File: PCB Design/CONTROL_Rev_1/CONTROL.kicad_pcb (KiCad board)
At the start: 2 copper layers, 40 x 80 mm, 42 parts, among them J1 Conn_01x24_Pin, J2 Conn_01x24_Pin, J3 Micro_SD_Card, P1 USB_C_Plug_USB2.0, SW1 SW_SPDT, U1 STM32F446RET6, Y1 16MHz, Y2 32.768KHz

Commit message: Completed Rev1 and Documentation
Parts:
- removed P1: USB_C_Plug_USB2.0, Connector_USB:USB_C_Receptacle_GCT_USB4085
- added D3: MINT, CONTROL:JB2835AWTWU57EA0000N0000001, F.Cu at (52.9, 157.6)
- added J4: USB_C_Receptacle_USB2.0_16P, Connector_USB:USB_C_Receptacle_GCT_USB4085, F.Cu at (75.6, 177.1)
- added R11: 5.1k, Resistor_SMD:R_0603_1608Metric, B.Cu at (73.9, 176.2)
- added R12: 5.1k, Resistor_SMD:R_0603_1608Metric, B.Cu at (78.4, 172.0)
- added R13: 1k, Resistor_SMD:R_0603_1608Metric, F.Cu at (52.8, 154.7)
- C1, C2, C3, C4, C5, C6, C7, C8, C9, R10, R2, R3, R4, R5, R6, R8, R9: moved to B.Cu
- C13, C14: footprint Capacitor_SMD:C_0603_1608Metric -> Capacitor_SMD:C_0402_1005Metric
- FB1: footprint Inductor_SMD:L_0201_0603Metric -> Inductor_SMD:L_0603_1608Metric; moved to B.Cu
- moved D1 22.5 mm to (62.1, 176.0), turned to -90 degrees
- moved R7 18.6 mm to (62.1, 173.0), turned to 180 degrees
- moved R5 13.2 mm to (51.5, 169.9), turned to 90 degrees
- moved R4 10.7 mm to (49.7, 171.7)
- moved R6 10.7 mm to (49.7, 168.5)
- moved R2 10.2 mm to (80.0, 148.4)
- moved C13 7.72 mm to (67.5, 145.0)
- moved C14 7.72 mm to (67.5, 143.3)
- moved C11 7.60 mm to (67.8, 140.3)
- moved C12 7.60 mm to (64.6, 140.3)
- moved Y1 7.60 mm to (65.3, 137.5)
- moved Y2 7.60 mm to (65.3, 144.2)
- moved R3 5.59 mm to (80.0, 152.6), turned to 90 degrees
- moved C1 4.09 mm to (70.3, 157.1), turned to -90 degrees
- moved C4 3.15 mm to (71.3, 166.1)
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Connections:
- net /LISTEN_EN renamed /PB5
- A1 pad 10: unconnected-(A1-GPIO7-Pad10) -> /GPIO_7
- A1 pad 11: unconnected-(A1-GPIO8-Pad11) -> /GPIO_8
- A1 pad 12: unconnected-(A1-GPIO9-Pad12) -> /GPIO_9
- A1 pad 14: unconnected-(A1-GPIO10-Pad14) -> /GPIO_10
- A1 pad 15: unconnected-(A1-GPIO11-Pad15) -> /GPIO_11
- A1 pad 16: unconnected-(A1-GPIO12-Pad16) -> /GPIO_12
- A1 pad 17: unconnected-(A1-GPIO13-Pad17) -> /GPIO_13
- A1 pad 19: unconnected-(A1-GPIO14-Pad19) -> /GPIO_14
- A1 pad 20: unconnected-(A1-GPIO15-Pad20) -> /GPIO_15
- A1 pad 21: unconnected-(A1-GPIO16-Pad21) -> /GPIO_16
- A1 pad 22: unconnected-(A1-GPIO17-Pad22) -> /GPIO_17
- A1 pad 24: unconnected-(A1-GPIO18-Pad24) -> /NRST
- A1 pad 25: unconnected-(A1-GPIO19-Pad25) -> /BOOT0
- A1 pad 26: unconnected-(A1-GPIO20-Pad26) -> /SWO
- A1 pad 27: unconnected-(A1-GPIO21-Pad27) -> /SWCLK
- A1 pad 29: unconnected-(A1-GPIO22-Pad29) -> /SWDIO
- A1 pad 31: unconnected-(A1-GPIO26_ADC0-Pad31) -> /GPIO_26
- A1 pad 32: unconnected-(A1-GPIO27_ADC1-Pad32) -> /GPIO_27
- A1 pad 34: unconnected-(A1-GPIO28_ADC2-Pad34) -> /GPIO_28
- A1 pad 9: unconnected-(A1-GPIO6-Pad9) -> /GPIO_6
- J1 pad 10: unconnected-(J1-Pin_10-Pad10) -> /GPIO_9
- J1 pad 11: unconnected-(J1-Pin_11-Pad11) -> /GPIO_10
- J1 pad 12: unconnected-(J1-Pin_12-Pad12) -> /GPIO_11
- J1 pad 13: unconnected-(J1-Pin_13-Pad13) -> /GPIO_12
- J1 pad 14: unconnected-(J1-Pin_14-Pad14) -> /GPIO_13
- J1 pad 15: /ADC1_IN0 -> /GPIO_14
- J1 pad 16: /ADC1_IN2 -> /ADC1_IN0
- J1 pad 18: /ADC1_IN3 -> /ADC1_IN2
- J1 pad 19: /PC4 -> /ADC1_IN3
- J1 pad 7: unconnected-(J1-Pin_7-Pad7) -> /GPIO_6
- J1 pad 8: unconnected-(J1-Pin_8-Pad8) -> /GPIO_7
- J1 pad 9: unconnected-(J1-Pin_9-Pad9) -> /GPIO_8
- J2 pad 10: unconnected-(J2-Pin_10-Pad10) -> /PB12
- J2 pad 11: unconnected-(J2-Pin_11-Pad11) -> /PB14
- J2 pad 12: unconnected-(J2-Pin_12-Pad12) -> /PB15
- J2 pad 13: unconnected-(J2-Pin_13-Pad13) -> /PC6
- J2 pad 14: unconnected-(J2-Pin_14-Pad14) -> /PC7
- J2 pad 4: unconnected-(J2-Pin_4-Pad4) -> /GPIO_28
- J2 pad 5: unconnected-(J2-Pin_5-Pad5) -> /GPIO_27
- J2 pad 6: unconnected-(J2-Pin_6-Pad6) -> /GPIO_26
- J2 pad 7: unconnected-(J2-Pin_7-Pad7) -> /GPIO_17
- J2 pad 8: unconnected-(J2-Pin_8-Pad8) -> /GPIO_16
- J2 pad 9: unconnected-(J2-Pin_9-Pad9) -> /PC4
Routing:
- net 3.3V: track 38.3 -> 234.6 mm, vias 0 -> 17
- net GND: track 16.5 -> 78.4 mm, vias 0 -> 124
- net /SWCLK: track 0.00 -> 59.2 mm, vias 0 -> 2
- net /PB12: track 0.00 -> 53.0 mm, vias 0 -> 1
- net /PB14: track 0.00 -> 50.0 mm, vias 0 -> 1
- net /SWDIO: track 0.00 -> 47.5 mm, vias 0 -> 2
- net /PB15: track 0.00 -> 47.2 mm, vias 0 -> 1
- net /PC6: track 0.00 -> 44.6 mm, vias 0 -> 1
- net /PC7: track 0.00 -> 42.2 mm, vias 0 -> 1
- net (no net): track 34.3 -> 0.00 mm, vias 25 -> 0
- net /GPIO_17: track 0.00 -> 32.4 mm
- net /GPIO_16: track 0.00 -> 32.4 mm
- net /PC4: track 21.9 -> 52.8 mm, vias 0 -> 1
- net /BOOT0: track 17.3 -> 46.9 mm, vias 2 -> 3
- net /SWO: track 0.00 -> 26.2 mm, vias 0 -> 1
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- added copper zone on B.Cu, net GND
- added copper zone on F.Cu, net GND
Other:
- board text added: "ADC1_IN0"
- board text added: "ADC1_IN1"
- board text added: "ADC1_IN2"
- board text added: "ADC1_IN3"
- board text added: "B0"
- board text added: "B1"
- board text added: "GPIO10"
- board text added: "GPIO11"
- board text added: "GPIO12"
- board text added: "GPIO13"
- board text added: "GPIO14"
- board text added: "GPIO16"
- board text added: "GPIO17"
- board text added: "GPIO26"
- board text added: "GPIO27"
- board text added: "GPIO28"
- board text added: "GPIO6"
- board text added: "GPIO7"
- board text added: "GPIO8"
- board text added: "GPIO9"
- board text added: "HI"
- board text added: "HI_B"
- board text added: "LI_A"
- board text added: "LI_B"
- board text added: "PA10"
- board text added: "PA9"
- board text added: "PB12"
- board text added: "PB14"
- board text added: "PB15"
- board text added: "PB5"
- board text added: "PB6"
- board text added: "PC4"
- board text added: "PC5"
- board text added: "PC6"
- board text added: "PC7"
- board text added: "PC8"
- board text added: "PC9"
- board text added: "PG_12"
- board text added: "PG_3.3"
- board text added: "PG_VPi"
- board text added: "SCL"
- board text added: "SDA"
- board text added: "V_Pi"
- board text removed: "PG_12V"
- board text removed: "PG_3.3V"
- board text removed: "PG_VPiezo"
- board text removed: "V_Piezo"

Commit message: Updated USB Port Schematic and PCB
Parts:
- added C21: 100n, Capacitor_SMD:C_0603_1608Metric, F.Cu at (69.0, 169.9)
- added R14: 100k, Resistor_SMD:R_0603_1608Metric, F.Cu at (72.9, 178.5)
- added U2: USBLC6-2SC6, Package_TO_SOT_SMD:SOT-23-6, F.Cu at (72.0, 170.5)
- moved R1 2.57 mm to (69.7, 174.5)
- moved SW1 2.53 mm to (67.5, 176.8)
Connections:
- J4 pad A4: unconnected-(J4-VBUS-PadA4) -> VBUS
- J4 pad A6: /USB_D+ -> /USB_D+IN
- J4 pad A7: /USB_D- -> /USB_D-IN
- J4 pad A9: unconnected-(J4-VBUS-PadA4)_3 -> VBUS
- J4 pad B4: unconnected-(J4-VBUS-PadA4)_1 -> VBUS
- J4 pad B6: /USB_D+ -> /USB_D+IN
- J4 pad B7: /USB_D- -> /USB_D-IN
- J4 pad B9: unconnected-(J4-VBUS-PadA4)_2 -> VBUS
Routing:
- net VBUS: track 0.00 -> 21.9 mm
- net /USB_D-: track 12.1 -> 4.21 mm
- net /USB_D-IN: track 0.00 -> 7.40 mm
- net /USB_D+IN: track 0.00 -> 6.36 mm
- net /USB_D+: track 12.5 -> 10.2 mm, vias 1 -> 2
- net /BOOT0: track 46.9 -> 49.0 mm
- net Net-(SW1-B): track 1.55 -> 0.00 mm
- net GND: track 78.4 -> 76.9 mm, vias 124 -> 123
- net 3.3V: track 234.6 -> 233.9 mm

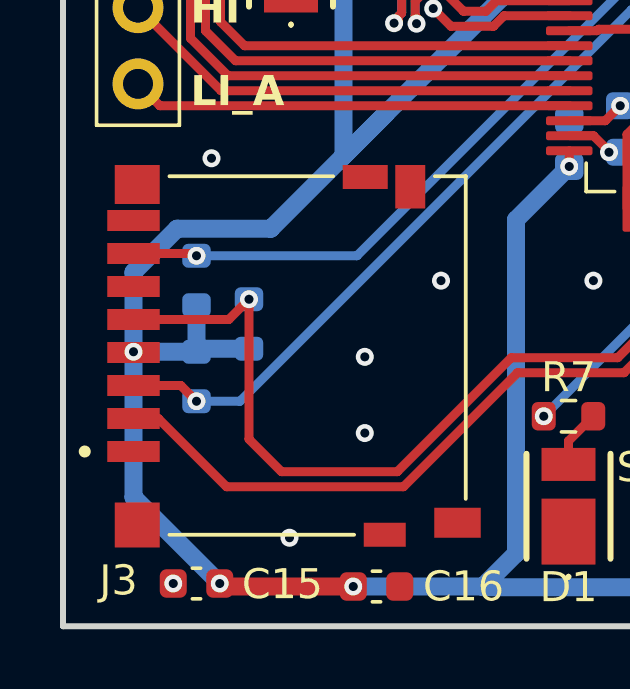
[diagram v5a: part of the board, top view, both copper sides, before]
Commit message: fix(sd-card): pull up unused DAT1 and DAT2 lines
- Add 47k pull-up resistors on DAT1 (pin 8) and DAT2 (pin 1) to 3.3V
- Required by SD spec to prevent undefined bus state during init
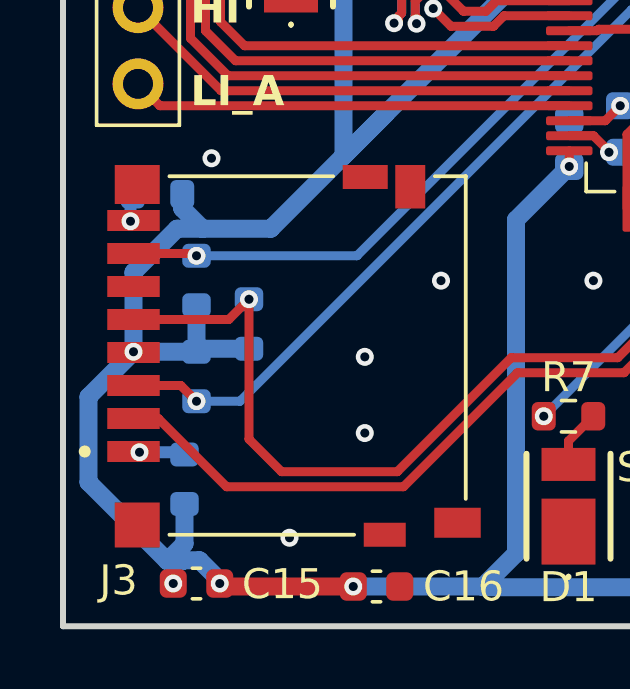
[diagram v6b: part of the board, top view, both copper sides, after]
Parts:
- added R15: 47k, Resistor_SMD:R_0603_1608Metric, B.Cu at (48.4, 165.6)
- added R16: 47k, Resistor_SMD:R_0603_1608Metric, B.Cu at (49.3, 175.1)
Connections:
- J3 pad 1: unconnected-(J3-DAT2-Pad1) -> /DAT2
- J3 pad 8: unconnected-(J3-DAT1-Pad8) -> /DAT1
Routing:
- net 3.3V: track 233.9 -> 239.3 mm
- net /DAT2: track 0.00 -> 1.74 mm, vias 0 -> 1
- net /DAT1: track 0.00 -> 1.04 mm, vias 0 -> 1

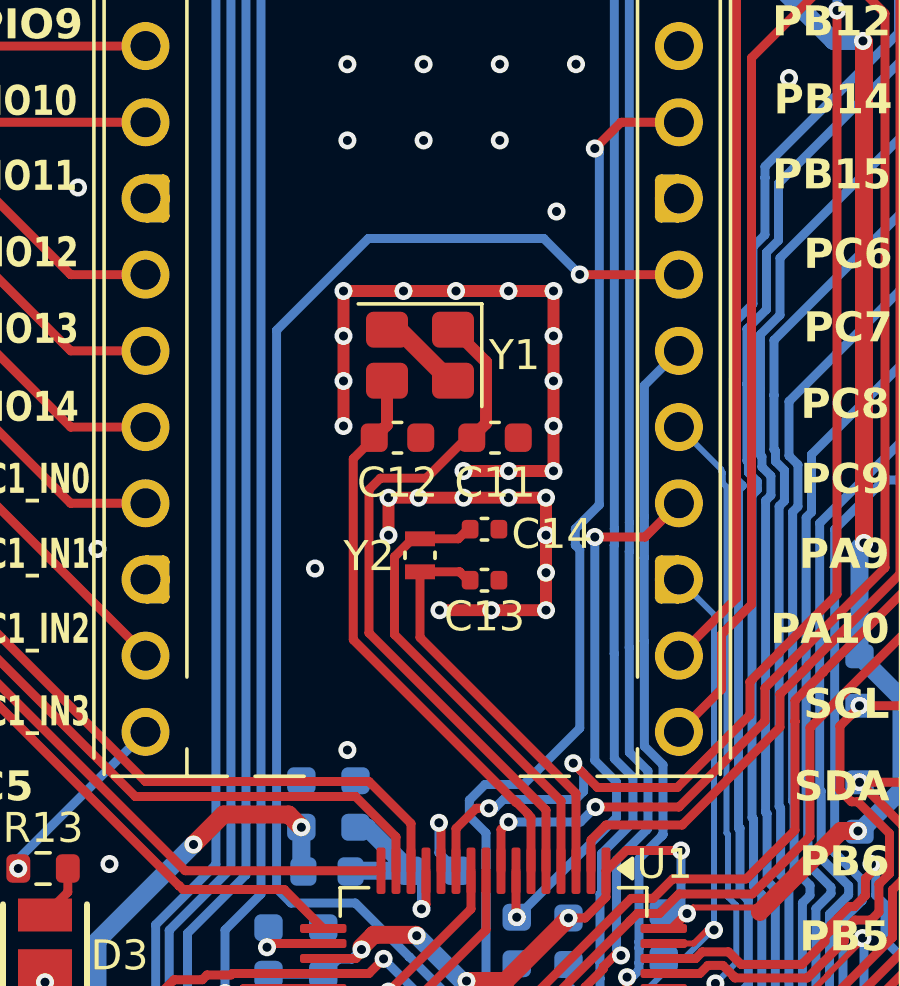
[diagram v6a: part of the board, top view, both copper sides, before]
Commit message: fix(crystals): correct LSE load cap configuration
- Remove C13 and C14 (1.2pF external load caps on LSE)
- ABS05W has CL = 4pF; use STM32 internal OSC caps instead
- HSE caps C11/C12 confirmed correct at 10pF for E3SB16E (CL = 8pF)
- Note: configure LSE drive to low-power mode in firmware to match ABS05W ESR
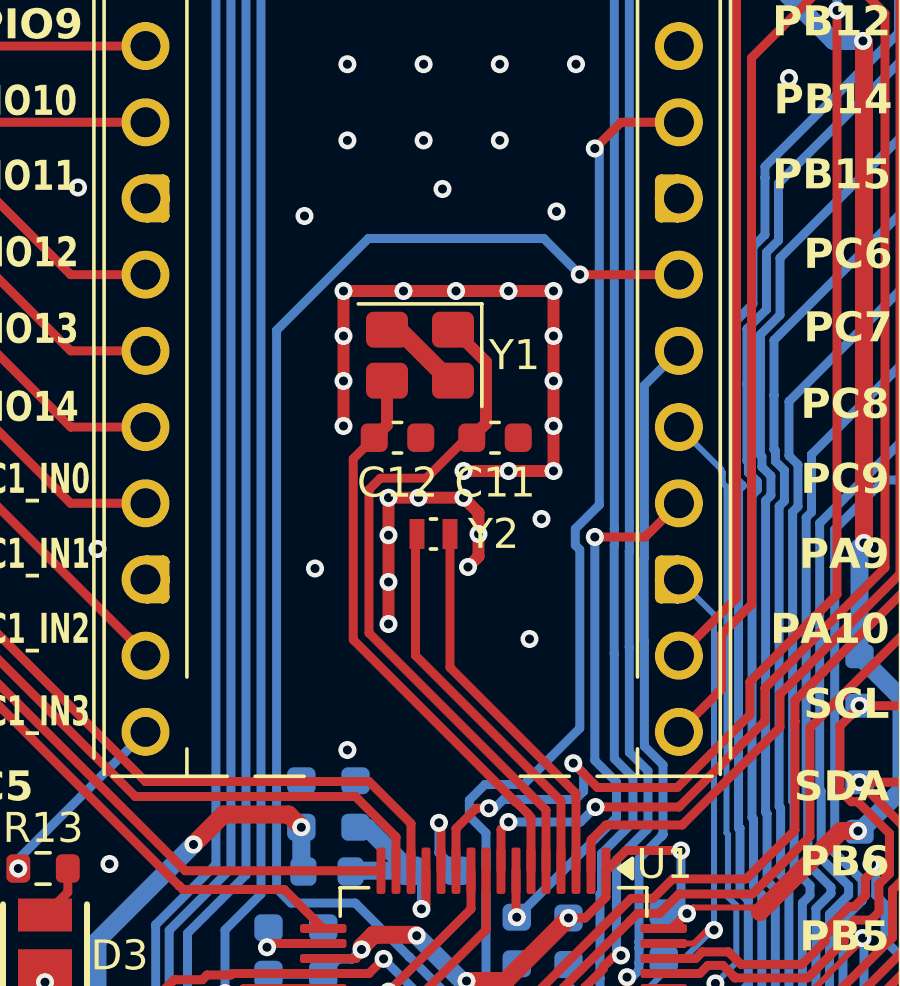
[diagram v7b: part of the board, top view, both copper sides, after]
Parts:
- removed C13, C14: 1.2p, Capacitor_SMD:C_0402_1005Metric
- moved Y2 0.84 mm to (65.8, 143.5), turned to 180 degrees
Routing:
- net GND: track 76.9 -> 72.5 mm, vias 123 -> 124
- net /LSE_OUT: track 15.8 -> 13.3 mm
- net /LSE_IN: track 13.8 -> 13.0 mm

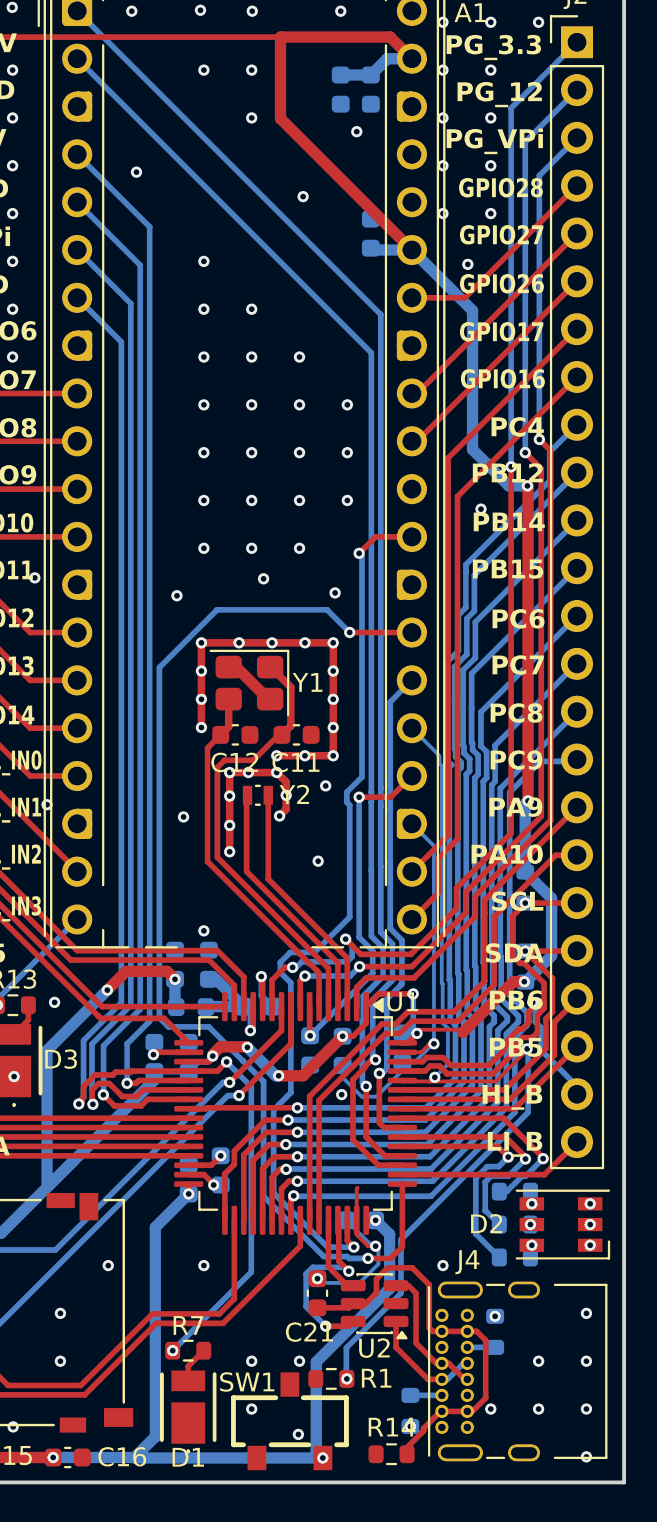
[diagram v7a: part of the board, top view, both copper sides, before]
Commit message: fix(pico): connect power pins and add reset pull-up
- Connect VSYS (pin 39) to 3.3V rail via header
- Connect 3V3_EN (pin 37) to 3.3V to keep regulator enabled
- Add 10k pull-up resistor on RUN (pin 30) to 3.3V
- Add no-connect on 3V3 (pin 36) — Pico regulator output unused
- Add no-connect on VBUS (pin 40) — USB power not used
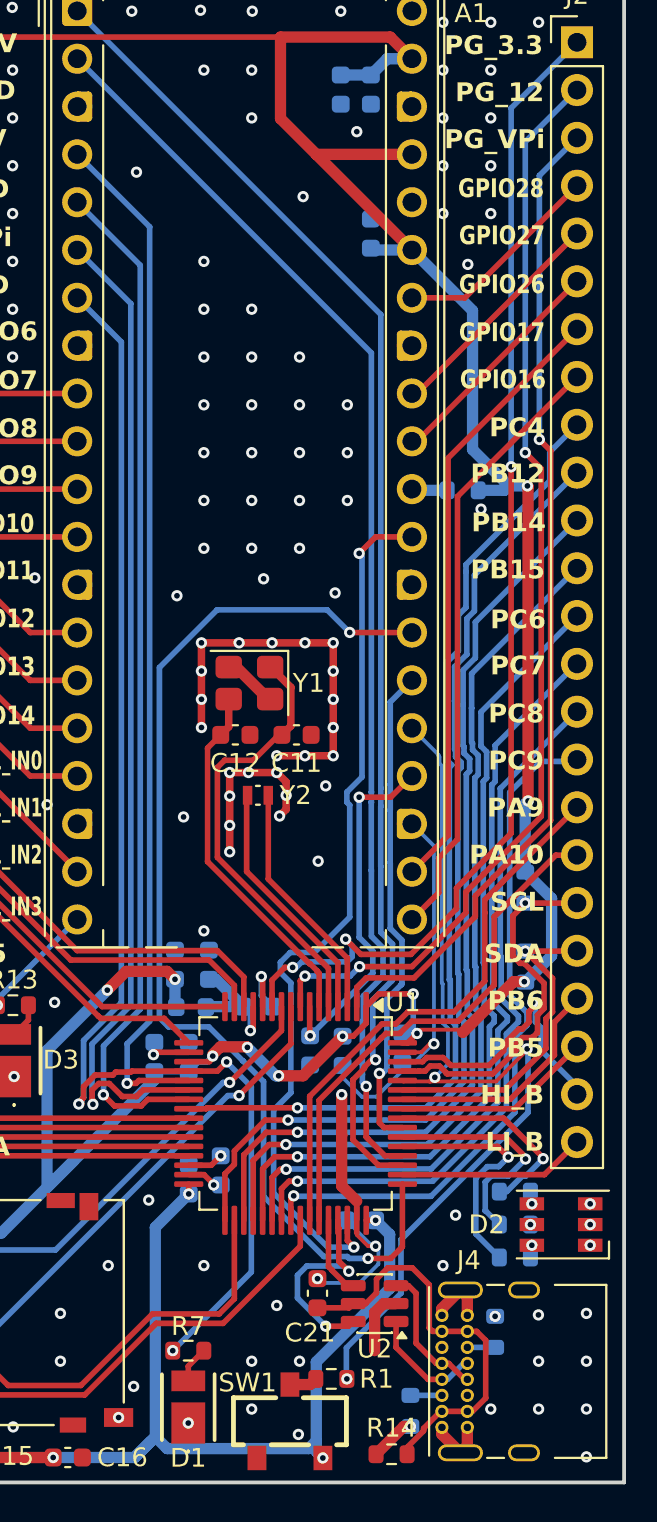
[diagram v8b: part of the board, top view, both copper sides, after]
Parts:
- added R17: 10k, Resistor_SMD:R_0603_1608Metric, B.Cu at (76.7, 127.3)
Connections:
- A1 pad 30: unconnected-(A1-RUN-Pad30) -> Net-(A1-RUN)
- A1 pad 37: unconnected-(A1-3V3_EN-Pad37) -> 3.3V
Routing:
- net GND: track 72.5 -> 90.0 mm, vias 124 -> 131
- net 3.3V: track 239.3 -> 246.4 mm
- net Net-(A1-RUN): track 0.00 -> 1.90 mm
- net Net-(SW1-B): track 0.00 -> 1.50 mm
- net /USB_D+: track 10.2 -> 10.9 mm
